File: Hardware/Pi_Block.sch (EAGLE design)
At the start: 51 parts, among them Q1 BSS138, U1 PCA9306, U2 EDISON_CONNECTOR_FULLMOUNTING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, U3 EDISON_CONNECTOR_FULLHEADER, U4 TPS62065, U5 MIC5219 3.3V

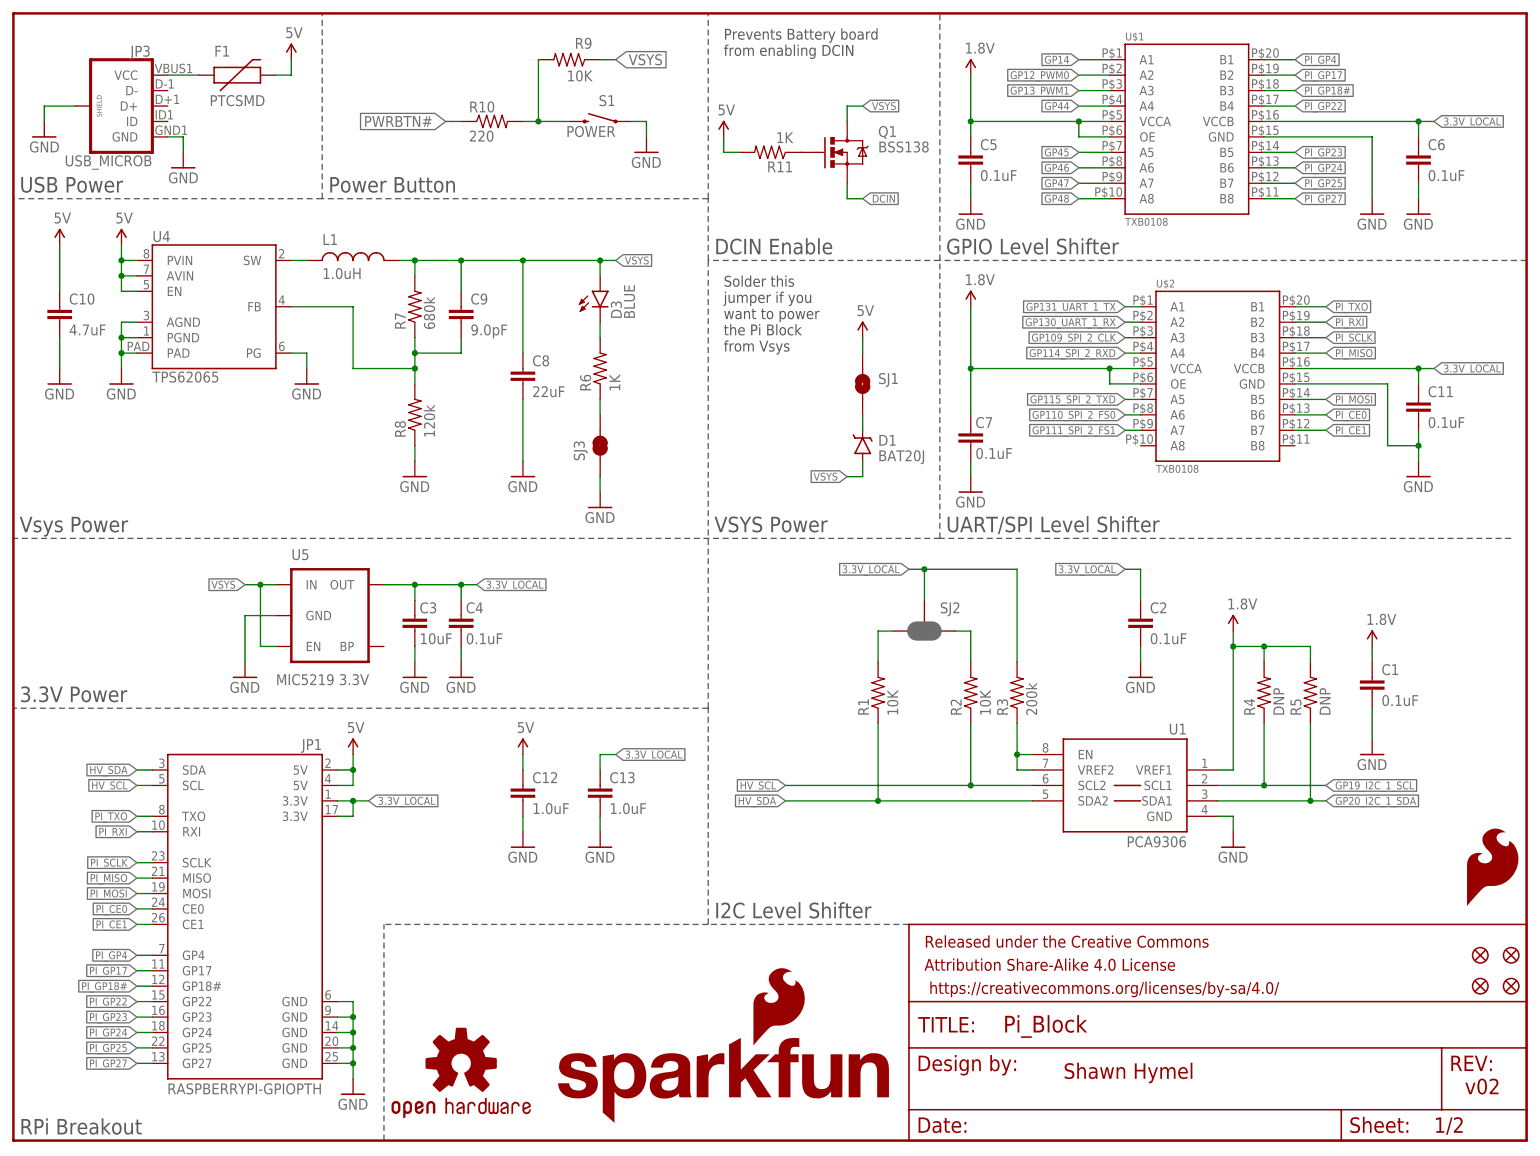
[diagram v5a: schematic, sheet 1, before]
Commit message: Added silk to Pi pins. Moved a few traces to straighten them or prevent bridging of pins.
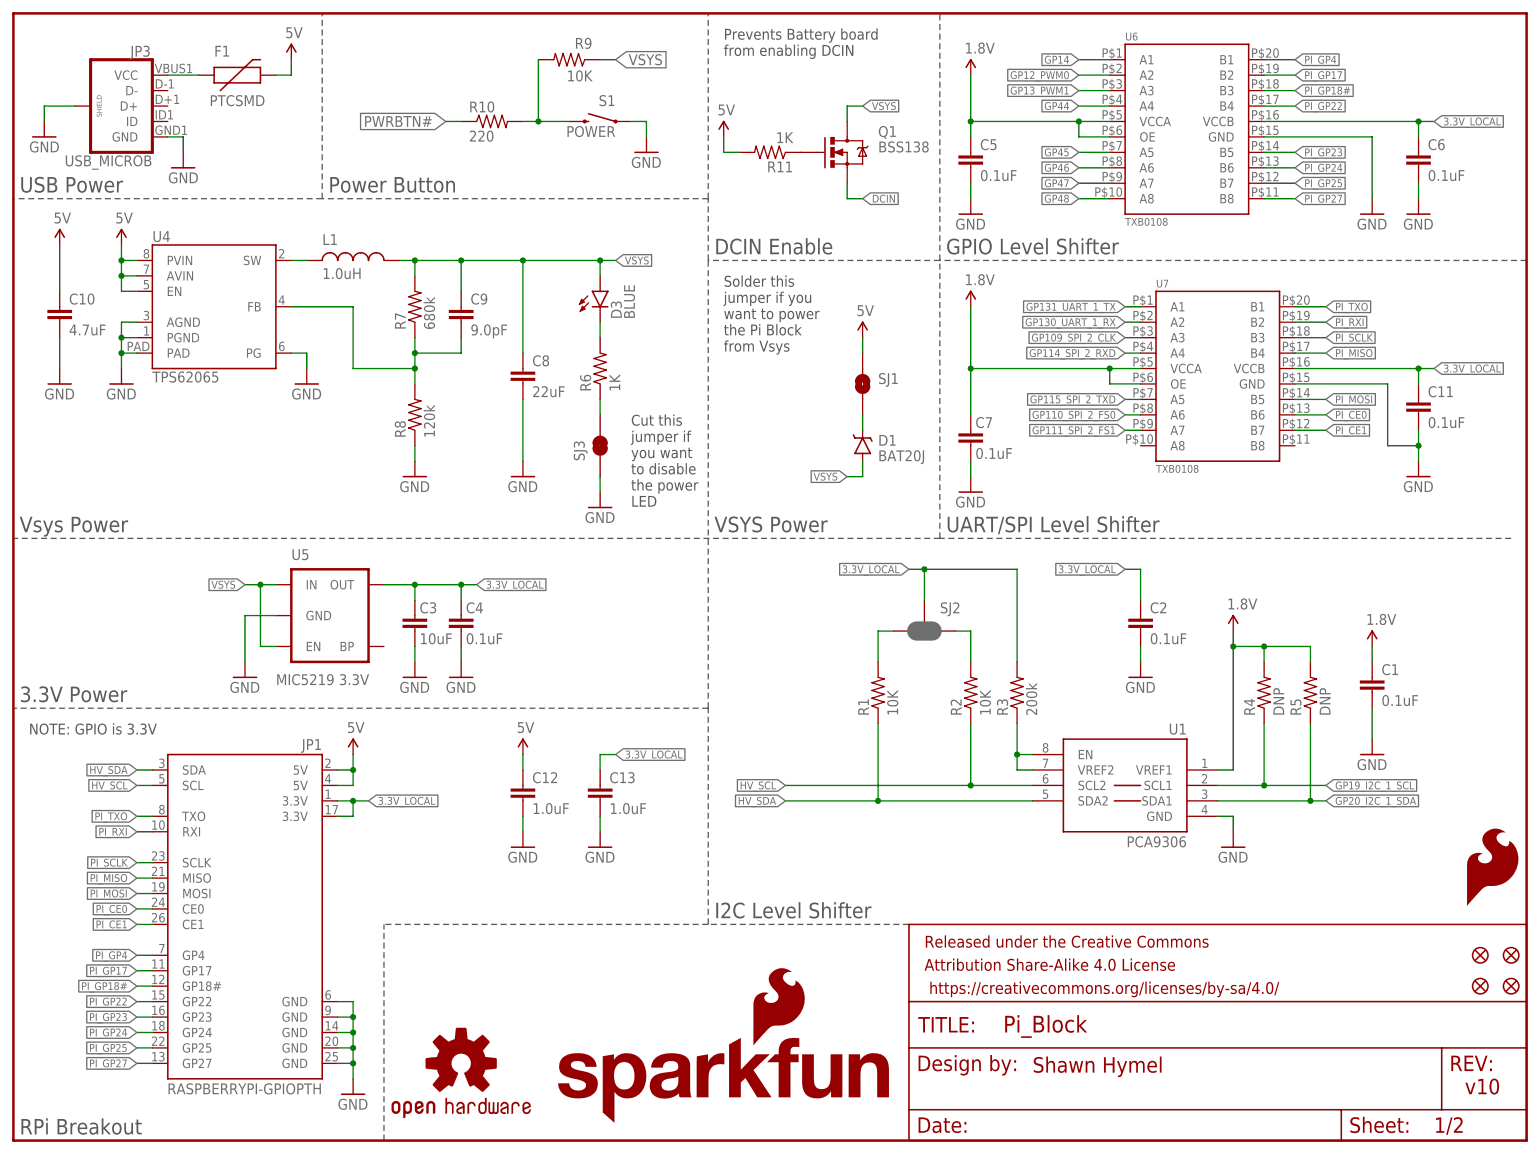
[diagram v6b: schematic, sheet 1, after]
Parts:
- renumbered U$1 to U6, U$2 to U7
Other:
- note added: "Cut this jumper if you want to disable the power LED"
- note added: "NOTE: GPIO is 3.3V"
- note added: "v10"
- note removed: "v02"

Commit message: Added ICs to SF lib. Added pin markers to ICs. Changed routing of TXB and PCA to come straight out pins. Added mounting hole below header. Added notes to board.
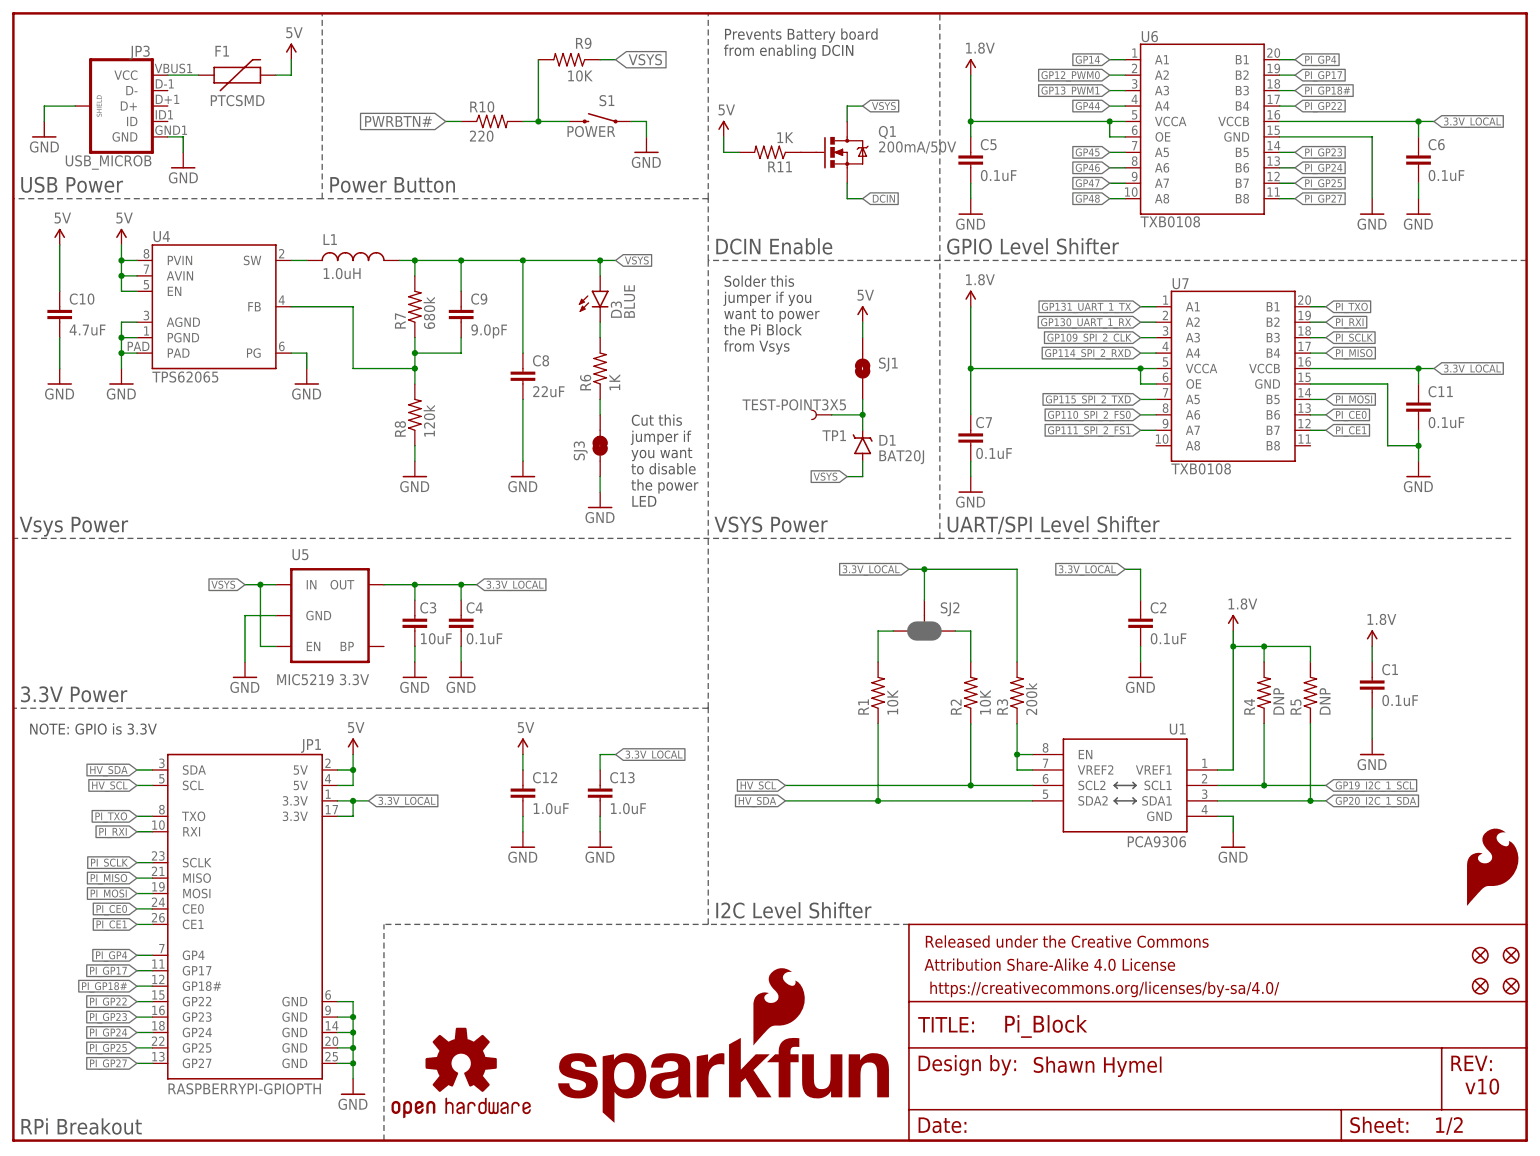
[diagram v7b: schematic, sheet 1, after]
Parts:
- added FRAME3: FRAME-LETTER, SparkFun-Aesthetics:FRAME-LETTER
- added TP1: TEST-POINT3X5, SparkFun-Passives:TEST-POINT3X5
- Q1: value BSS138 -> 200mA/50V
- R1, R2, R9: device SparkFun-Resistors:10KOHM1/10W1%(0603)0603 -> SparkFun-Resistors:10KOHM-1/10W-1%(0603)0603
- R11, R6: device SparkFun-Resistors:1KOHM1/10W1%(0603) -> SparkFun-Resistors:1KOHM-1/10W-1%(0603)
- U4: device Testing:TPS62065 -> SparkFun-PowerIC:TPS62065
- U6, U7: device Testing:TXB0108 -> SparkFun-DigitalIC:TXB0108
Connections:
- net N$3: now also TP1.1
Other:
- moved on the sheet: SJ1, U6, U7

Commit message: Corrected errors from review and QC check (see GitHub issues)
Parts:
- R7: PROD_ID (none) -> RES-12280
- R8: PROD_ID (none) -> RES-12279
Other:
- note added: "NOTES: - Board thickness = 0.063 in."
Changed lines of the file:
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@@
 <setting verticaltext="up"/>
 </settings>
-<grid distance="0.1" unitdist="inch" unit="inch" style="lines" multiple="1" display="no" altdistance="0.01" altunitdist="inch" altunit="inch"/>
+<grid distance="0.1" unitdist="inch" unit="inch" style="lines" multiple="1" display="yes" altdistance="0.01" altunitdist="inch" altunit="inch"/>
 <layers>
 <layer number="1" name="Top" color="4" fill="1" visible="no" active="no"/>
@@
 <part name="GND22" library="SparkFun-Aesthetics" deviceset="GND" device=""/>
 <part name="SUPPLY11" library="SparkFun-Aesthetics" deviceset="5V" device=""/>
-<part name="R7" library="SparkFun-Resistors" deviceset="RESISTOR" device="0603" value="680k"/>
-<part name="R8" library="SparkFun-Resistors" deviceset="RESISTOR" device="0603" value="120k"/>
+<part name="R7" library="SparkFun-Resistors" deviceset="RESISTOR" device="0603" value="680k">
+<attribute name="PROD_ID" value="RES-12280"/>
+</part>
+<part name="R8" library="SparkFun-Resistors" deviceset="RESISTOR" device="0603" value="120k">
+<attribute name="PROD_ID" value="RES-12279"/>
+</part>
 <part name="C9" library="SparkFun-Capacitors" deviceset="9.0PF-50V-10%(0603)" device="" value="9.0pF"/>
 <part name="C10" library="SparkFun-Capacitors" deviceset="4.7UF-6.3V-10%(0603)" device="0603" value="4.7uF"/>
@@
 LED</text>
 <text x="2.54" y="68.58" size="1.778" layer="97" align="top-left">NOTE: GPIO is 3.3V</text>
+<text x="63.5" y="33.02" size="2.54" layer="97" align="top-left">NOTES:
+ - Board thickness = 0.063 in.</text>
 </plain>
 <instances>
@@
 <instance part="GND22" gate="1" x="48.26" y="124.46"/>
 <instance part="SUPPLY11" gate="G$1" x="7.62" y="147.32"/>
-<instance part="R7" gate="G$1" x="66.04" y="137.16" rot="R90"/>
-<instance part="R8" gate="G$1" x="66.04" y="119.38" rot="R90"/>
+<instance part="R7" gate="G$1" x="66.04" y="137.16" rot="R90">
+<attribute name="PROD_ID" x="66.04" y="137.16" size="1.778" layer="96" rot="R90" display="off"/>
+</instance>
+<instance part="R8" gate="G$1" x="66.04" y="119.38" rot="R90">
+<attribute name="PROD_ID" x="66.04" y="119.38" size="1.778" layer="96" rot="R90" display="off"/>
+</instance>
 <instance part="C9" gate="G$1" x="73.66" y="134.62"/>
 <instance part="C10" gate="G$1" x="7.62" y="134.62"/>
